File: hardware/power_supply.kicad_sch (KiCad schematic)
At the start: 25 parts, among them J2 POWER, U10 NCP1117-5.0, U11 LM2596DS-ADJ, U12 NCP1117-3.3, U13 NCP1117-3.3, U14 NCP1117-3.3

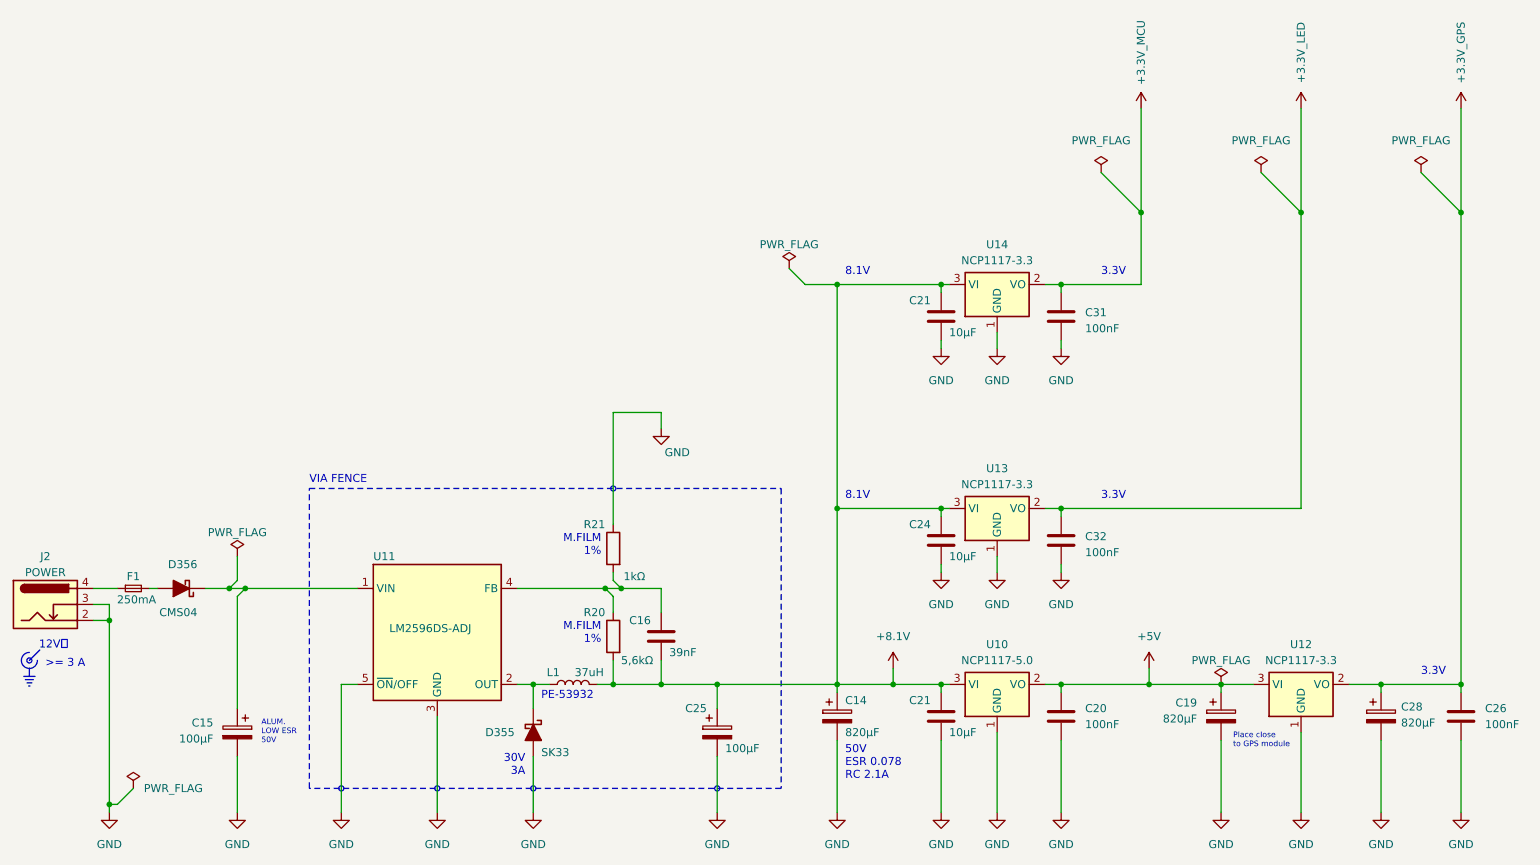
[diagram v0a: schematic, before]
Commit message: Updated project to work with KiCAD version 9
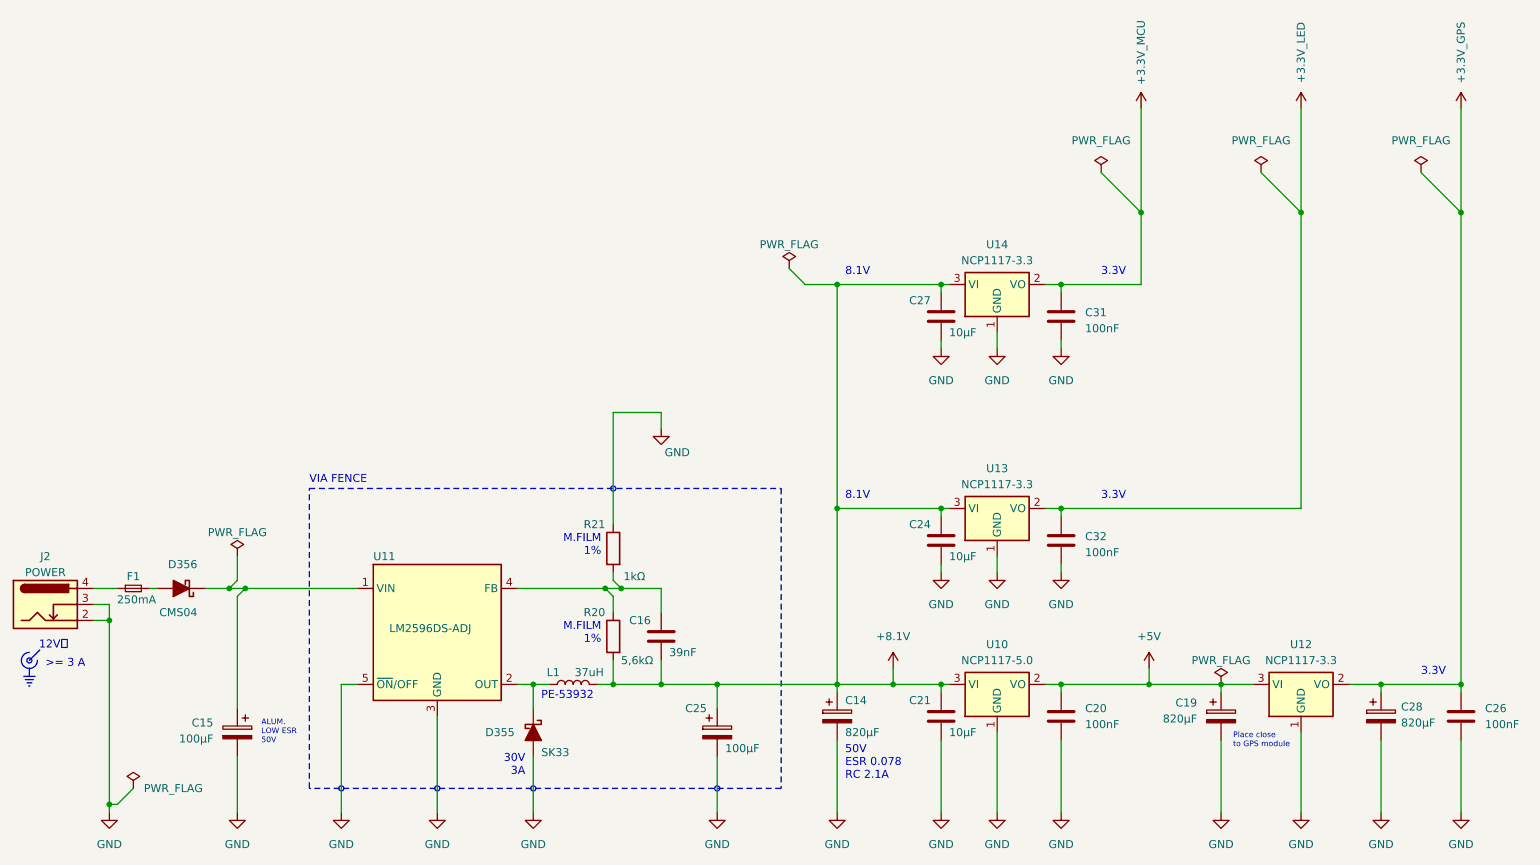
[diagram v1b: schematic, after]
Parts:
- U11: footprint Regulator_SMD_mouser:NCP5663DSADJR4G -> Package_TO_SOT_THT:TO-220-5_P3.4x3.7mm_StaggerOdd_Lead3.8mm_Vertical
- renumbered C21 to C27
